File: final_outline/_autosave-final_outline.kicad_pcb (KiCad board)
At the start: 2 copper layers, 99.8 x 101.8 mm, 33 parts, among them P001 CANCONNECTOR, P002 AUXCONNECTOR, P100 ISP, P101 DEBUG_LED, U401 ISO1050, U402 ISO1050, U403 LPC11C14, U404 MCP2515_TSSOP, U405 ISO1050, U501 MCP1755

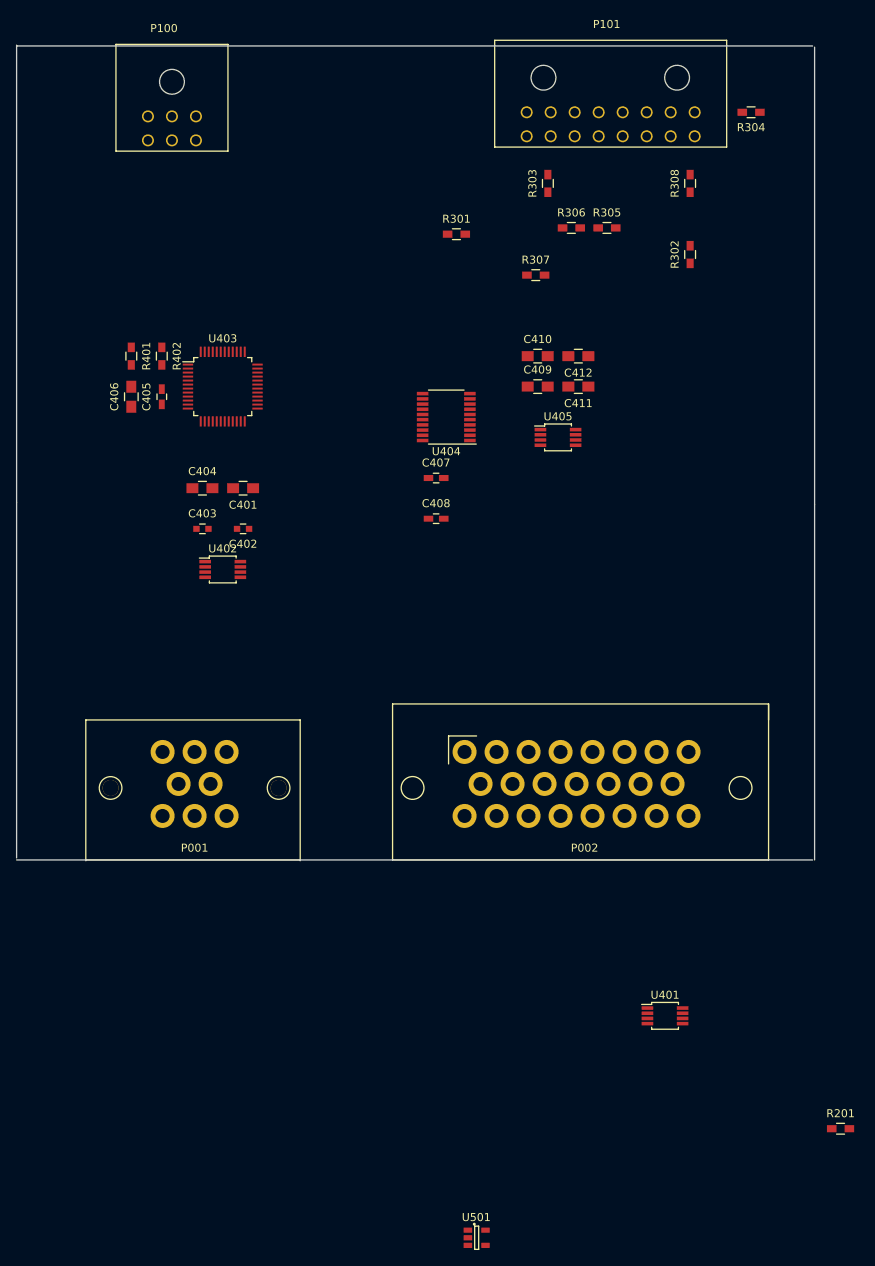
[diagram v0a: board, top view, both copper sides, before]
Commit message: Working on connections between sheets, deleted CAN2
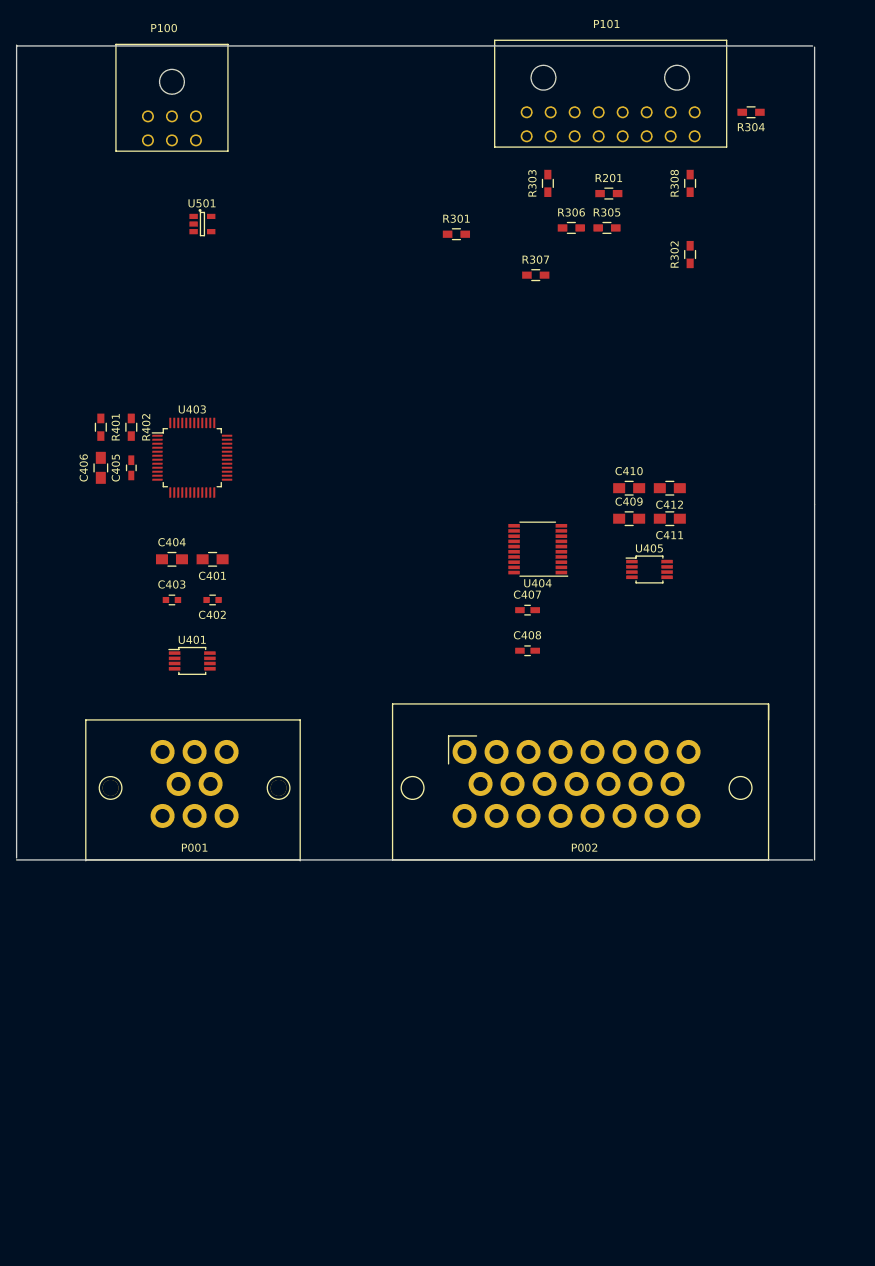
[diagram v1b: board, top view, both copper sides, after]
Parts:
- removed U402: ISO1050, Housings_SSOP:MSOP-8_3x3mm_Pitch0.65mm
- moved U501 131.3 mm to (125.7, 48.3)
- moved R201 120.4 mm to (176.5, 44.5)
- moved U401 73.9 mm to (124.5, 102.9)
- moved C409 20.1 mm to (179.1, 85.1)
- moved C410 20.1 mm to (179.1, 81.3)
- moved C411 20.1 mm to (184.2, 85.1)
- moved C412 20.1 mm to (184.2, 81.3)
- moved C407 20.1 mm to (166.4, 96.5)
- moved C408 20.1 mm to (166.4, 101.6)
- moved U405 20.1 mm to (181.6, 91.4)
- moved U404 20.1 mm to (167.6, 88.9)
- moved U403 9.67 mm to (124.5, 77.5)
- moved C401 9.67 mm to (127.0, 90.2)
- moved C402 9.67 mm to (127.0, 95.2)
- moved C403 9.67 mm to (121.9, 95.2)
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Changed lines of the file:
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@@
 (kicad_pcb (version 4) (host pcbnew "(2015-10-29 BZR 6286)-product")
   (general
-    (links 83)
-    (no_connects 83)
+    (links 75)
+    (no_connects 75)
     (area 102.424999 25.824999 202.325001 127.825001)
     (thickness 1.6)
@@
     (tracks 0)
     (zones 0)
-    (modules 33)
+    (modules 32)
     (nets 114)
   )
@@
   )
   (module Capacitors_SMD:C_0805_HandSoldering (layer F.Cu)
-    (at 130.81 81.28 180)
+    (at 127 90.17 180)
     (descr "Capacitor SMD 0805, hand soldering")
     (tags "capacitor 0805")
@@
   )
   (module Capacitors_SMD:C_0603 (layer F.Cu)
-    (at 130.81 86.36 180)
+    (at 127 95.25 180)
     (descr "Capacitor SMD 0603, reflow soldering, AVX (see smccp.pdf)")
     (tags "capacitor 0603")
@@
   )
   (module Capacitors_SMD:C_0603 (layer F.Cu)
-    (at 125.73 86.36)
+    (at 121.92 95.25)
     (descr "Capacitor SMD 0603, reflow soldering, AVX (see smccp.pdf)")
     (tags "capacitor 0603")
@@
   )
   (module Capacitors_SMD:C_0805_HandSoldering (layer F.Cu)
-    (at 125.73 81.28)
+    (at 121.92 90.17)
     (descr "Capacitor SMD 0805, hand soldering")
     (tags "capacitor 0805")
@@
   )
   (module Capacitors_SMD:C_0603_HandSoldering (layer F.Cu)
-    (at 120.65 69.85 90)
+    (at 116.84 78.74 90)
     (descr "Capacitor SMD 0603, hand soldering")
     (tags "capacitor 0603")
@@
   )
   (module Capacitors_SMD:C_0805_HandSoldering (layer F.Cu)
-    (at 116.84 69.85 90)
+    (at 113.03 78.74 90)
     (descr "Capacitor SMD 0805, hand soldering")
     (tags "capacitor 0805")
@@
   )
   (module Capacitors_SMD:C_0603_HandSoldering (layer F.Cu)
-    (at 154.94 80.01)
+    (at 166.37 96.52)
     (descr "Capacitor SMD 0603, hand soldering")
     (tags "capacitor 0603")
@@
   )
   (module Capacitors_SMD:C_0603_HandSoldering (layer F.Cu)
-    (at 154.94 85.09)
+    (at 166.37 101.6)
     (descr "Capacitor SMD 0603, hand soldering")
     (tags "capacitor 0603")
@@
   )
   (module Capacitors_SMD:C_0805_HandSoldering (layer F.Cu)
-    (at 167.64 68.58)
+    (at 179.07 85.09)
     (descr "Capacitor SMD 0805, hand soldering")
     (tags "capacitor 0805")
@@
   )
   (module Capacitors_SMD:C_0805_HandSoldering (layer F.Cu)
-    (at 167.64 64.77)
+    (at 179.07 81.28)
     (descr "Capacitor SMD 0805, hand soldering")
     (tags "capacitor 0805")
@@
   )
   (module Capacitors_SMD:C_0805_HandSoldering (layer F.Cu)
-    (at 172.72 68.58 180)
+    (at 184.15 85.09 180)
     (descr "Capacitor SMD 0805, hand soldering")
     (tags "capacitor 0805")
@@
   )
   (module Capacitors_SMD:C_0805_HandSoldering (layer F.Cu)
-    (at 172.72 64.77 180)
+    (at 184.15 81.28 180)
     (descr "Capacitor SMD 0805, hand soldering")
     (tags "capacitor 0805")
@@
   )
   (module Resistors_SMD:R_0603_HandSoldering (layer F.Cu)
-    (at 205.495001 161.345)
+    (at 176.53 44.45)
     (descr "Resistor SMD 0603, hand soldering")
     (tags "resistor 0603")
@@
   )
   (module Resistors_SMD:R_0603_HandSoldering (layer F.Cu)
-    (at 116.84 64.77 270)
+    (at 113.03 73.66 270)
     (descr "Resistor SMD 0603, hand soldering")
     (tags "resistor 0603")
@@
   )
   (module Resistors_SMD:R_0603_HandSoldering (layer F.Cu)
-    (at 120.65 64.77 270)
+    (at 116.84 73.66 270)
     (descr "Resistor SMD 0603, hand soldering")
     (tags "resistor 0603")
@@
   )
   (module Housings_SSOP:MSOP-8_3x3mm_Pitch0.65mm (layer F.Cu)
-    (at 183.555001 147.235)
+    (at 124.46 102.87)
     (descr "8-Lead Plastic Micro Small Outline Package (MS) [MSOP] (see Microchip Packaging Specification 00000049BS.pdf)")
     (tags "SSOP 0.65")
@@
     )
   )
-  (module Housings_SSOP:MSOP-8_3x3mm_Pitch0.65mm (layer F.Cu)
-    (at 128.27 91.44)
-    (descr "8-Lead Plastic Micro Small Outline Package (MS) [MSOP] (see Microchip Packaging Specification 00000049BS.pdf)")
-    (tags "SSOP 0.65")
-    (attr smd)
-    (fp_text reference U402 (at 0 -2.6) (layer F.SilkS)
-      (effects (font (size 1 1) (thickness 0.15)))
-    )
-    (fp_text value ISO1050 (at 0 2.6) (layer F.Fab)
-      (effects (font (size 1 1) (thickness 0.15)))
-    )
-    (fp_line (start -3.2 -1.85) (end -3.2 1.85) (layer F.CrtYd) (width 0.05))
-    (fp_line (start 3.2 -1.85) (end 3.2 1.85) (layer F.CrtYd) (width 0.05))
-    (fp_line (start -3.2 -1.85) (end 3.2 -1.85) (layer F.CrtYd) (width 0.05))
-    (fp_line (start -3.2 1.85) (end 3.2 1.85) (layer F.CrtYd) (width 0.05))
-    (fp_line (start -1.675 -1.675) (end -1.675 -1.425) (layer F.SilkS) (width 0.15))
-    (fp_line (start 1.675 -1.675) (end 1.675 -1.425) (layer F.SilkS) (width 0.15))
-    (fp_line (start 1.675 1.675) (end 1.675 1.425) (layer F.SilkS) (width 0.15))
-    (fp_line (start -1.675 1.675) (end -1.675 1.425) (layer F.SilkS) (width 0.15))
-    (fp_line (start -1.675 -1.675) (end 1.675 -1.675) (layer F.SilkS) (width 0.15))
-    (fp_line (start -1.675 1.675) (end 1.675 1.675) (layer F.SilkS) (width 0.15))
-    (fp_line (start -1.675 -1.425) (end -2.925 -1.425) (layer F.SilkS) (width 0.15))
-    (pad 1 smd rect (at -2.2 -0.975) (size 1.45 0.45) (layers F.Cu F.Paste F.Mask)
-      (net 36 +3V3))
-    (pad 2 smd rect (at -2.2 -0.325) (size 1.45 0.45) (layers F.Cu F.Paste F.Mask)
-      (net 53 "Net-(U401-Pad2)"))
-    (pad 3 smd rect (at -2.2 0.325) (size 1.45 0.45) (layers F.Cu F.Paste F.Mask)
-      (net 54 "Net-(U401-Pad3)"))
-    (pad 4 smd rect (at -2.2 0.975) (size 1.45 0.45) (layers F.Cu F.Paste F.Mask)
-      (net 35 GND))
-    (pad 5 smd rect (at 2.2 0.975) (size 1.45 0.45) (layers F.Cu F.Paste F.Mask)
-      (net 35 GND))
-    (pad 6 smd rect (at 2.2 0.325) (size 1.45 0.45) (layers F.Cu F.Paste F.Mask)
-      (net 55 /Micro_Controller/CAN1L))
-    (pad 7 smd rect (at 2.2 -0.325) (size 1.45 0.45) (layers F.Cu F.Paste F.Mask)
-      (net 56 /Micro_Controller/CAN1H))
-    (pad 8 smd rect (at 2.2 -0.975) (size 1.45 0.45) (layers F.Cu F.Paste F.Mask)
-      (net 34 /Micro_Controller/CAN1P))
-    (model Housings_SSOP.3dshapes/MSOP-8_3x3mm_Pitch0.65mm.wrl
-      (at (xyz 0 0 0))
-      (scale (xyz 1 1 1))
-      (rotate (xyz 0 0 0))
-    )
-  )
   (module Housings_QFP:LQFP-48_7x7mm_Pitch0.5mm (layer F.Cu)
-    (at 128.27 68.58)
+    (at 124.46 77.47)
     (descr "48 LEAD LQFP 7x7mm (see MICREL LQFP7x7-48LD-PL-1.pdf)")
     (tags "QFP 0.5")
@@
   )
   (module Housings_SSOP:TSSOP-20_4.4x6.5mm_Pitch0.65mm (layer F.Cu)
-    (at 156.21 72.39 180)
+    (at 167.64 88.9 180)
     (descr "20-Lead Plastic Thin Shrink Small Outline (ST)-4.4 mm Body [TSSOP] (see Microchip Packaging Specification 00000049BS.pdf)")
     (tags "SSOP 0.65")
@@
   )
   (module Housings_SSOP:MSOP-8_3x3mm_Pitch0.65mm (layer F.Cu)
-    (at 170.18 74.93)
+    (at 181.61 91.44)
     (descr "8-Lead Plastic Micro Small Outline Package (MS) [MSOP] (see Microchip Packaging Specification 00000049BS.pdf)")
     (tags "SSOP 0.65")
@@
   )
   (module Housings_SOT-23_SOT-143_TSOT-6:SOT-23-5 (layer F.Cu)
-    (at 160.01119 174.975)
+    (at 125.73 48.26)
     (descr "5-pin SOT23 package")
     (tags SOT-23-5)

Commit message: final_outline: updated debug LED pin assignments on schematic
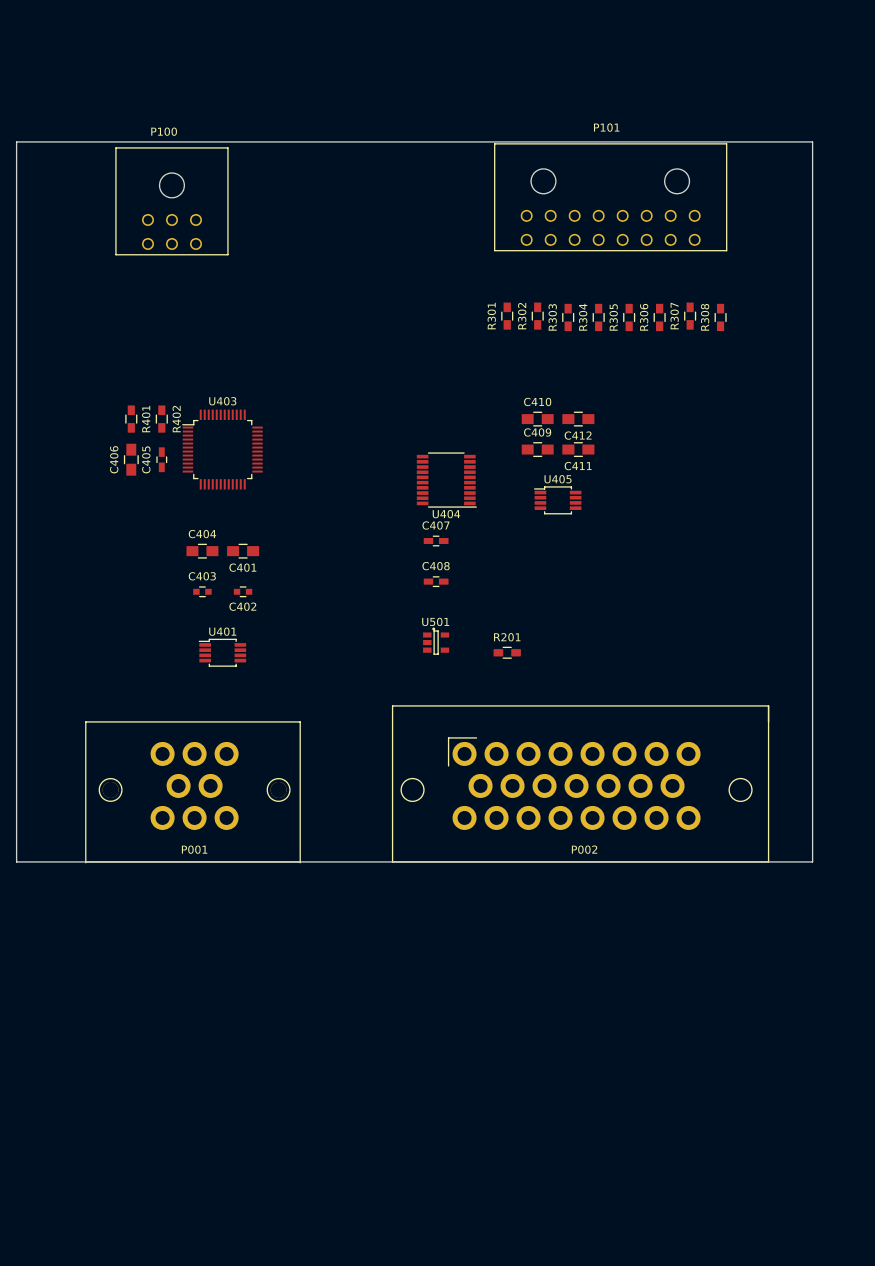
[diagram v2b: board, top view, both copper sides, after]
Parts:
- moved U501 59.9 mm to (154.9, 100.6)
- moved R201 58.8 mm to (163.8, 101.8)
- moved R304 32.0 mm to (175.3, 59.9), turned to 90 degrees
- moved R302 20.5 mm to (167.6, 59.8)
- moved R307 20.0 mm to (186.7, 59.8), turned to 90 degrees
- moved R308 17.2 mm to (190.5, 59.9)
- moved R303 17.0 mm to (171.4, 59.9)
- moved R306 15.7 mm to (182.9, 59.9), turned to 90 degrees
- moved C407 14.3 mm to (154.9, 87.9)
- moved C408 14.3 mm to (154.9, 93.0)
- moved C409 14.3 mm to (167.6, 76.5)
- moved C410 14.3 mm to (167.6, 72.6)
- moved C411 14.3 mm to (172.7, 76.5)
- moved C412 14.3 mm to (172.7, 72.6)
- moved U405 14.3 mm to (170.2, 82.8)
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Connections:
- C401 pad 1: /Micro_Controller/CAN1P -> /BACK_PANEL/CANH
- C402 pad 1: /Micro_Controller/CAN1P -> /BACK_PANEL/CANH
- C403 pad 1: +3V3 -> /Micro_Controller/+3V3
- C404 pad 1: +3V3 -> /Micro_Controller/+3V3
- C405 pad 1: +3V3 -> /Micro_Controller/+3V3
- C406 pad 1: +3V3 -> /Micro_Controller/+3V3
- R401 pad 1: +3V3 -> /Micro_Controller/+3V3
- R401 pad 2: /Micro_Controller/MCU_RESET_N -> /FRONT_PANEL/MCU_RESET_N
- R402 pad 1: +3V3 -> /Micro_Controller/+3V3
- R402 pad 2: /Micro_Controller/MCU_RESET_N -> /FRONT_PANEL/MCU_PROG_N
- U401 pad 1: +3V3 -> /Micro_Controller/+3V3
- U401 pad 6: /Micro_Controller/CAN1L -> GND
- U401 pad 7: /Micro_Controller/CAN1H -> /BACK_PANEL/CANH
- U401 pad 8: /Micro_Controller/CAN1P -> /BACK_PANEL/CANH
- U403 pad 1: /Micro_Controller/LED1 -> /FRONT_PANEL/LED1
- U403 pad 11: /Micro_Controller/LED2 -> /FRONT_PANEL/LED2
- U403 pad 12: /Micro_Controller/LED3 -> /FRONT_PANEL/LED3
- U403 pad 3: /Micro_Controller/MCU_RESET_N -> /FRONT_PANEL/MCU_RESET_N
- U403 pad 36: /Micro_Controller/LED4 -> /FRONT_PANEL/LED4
- U403 pad 37: /Micro_Controller/LED5 -> /FRONT_PANEL/LED5
- U403 pad 4: /Micro_Controller/MCU_RESET_N -> /FRONT_PANEL/MCU_PROG_N
- U403 pad 43: /Micro_Controller/LED6 -> /FRONT_PANEL/LED6
- U403 pad 44: +3V3 -> /Micro_Controller/+3V3
- U403 pad 46: /Micro_Controller/RXD -> /FRONT_PANEL/RXD
- U403 pad 47: /Micro_Controller/TXD -> /FRONT_PANEL/TXD
- U403 pad 48: /Micro_Controller/LED7 -> /FRONT_PANEL/LED7
- U403 pad 8: +3V3 -> /Micro_Controller/+3V3
- U403 pad 9: /Micro_Controller/LED0 -> /FRONT_PANEL/LED0
- U501 pad 1: /Power_Supplies/+5V -> /FRONT_PANEL/+5V
- U501 pad 3: /Power_Supplies/+5V -> /FRONT_PANEL/+5V
- U501 pad 5: /Power_Supplies/+3V3 -> /Micro_Controller/+3V3
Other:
- board size 99.8 x 101.8 mm -> 99.5 x 90 mm
